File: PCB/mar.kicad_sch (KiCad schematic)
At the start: 17 parts, among them SW3 SW_DIP_x04, SW4 SW_SPDT, U18 74LS157, U19 74LS173

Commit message: Cleaned up the schematic and got started on assigning all the footprints to the symbols
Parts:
- C11: footprint (none) -> Capacitor_THT:C_Radial_D5.0mm_H5.0mm_P2.00mm
- D20, D21, D22, D23, D24, D25: footprint (none) -> LED_THT:LED_D1.8mm_W1.8mm_H2.4mm_Horizontal_O1.27mm_Z1.6mm
- R18, R19, R20, R21, R22, R23: footprint (none) -> Resistor_THT:R_Axial_DIN0207_L6.3mm_D2.5mm_P7.62mm_Horizontal
- SW3: footprint (none) -> Button_Switch_THT:SW_DIP_SPSTx04_Slide_6.7x11.72mm_W7.62mm_P2.54mm_LowProfile
- SW4: footprint (none) -> Button_Switch_SMD:SW_SPDT_CK_JS102011SAQN
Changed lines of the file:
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@@
 			)
 		)
-		(property "Footprint" ""
+		(property "Footprint" "Resistor_THT:R_Axial_DIN0207_L6.3mm_D2.5mm_P7.62mm_Horizontal"
 			(at 41.402 49.53 90)
 			(effects
@@
 			)
 		)
-		(property "Footprint" ""
+		(property "Footprint" "Resistor_THT:R_Axial_DIN0207_L6.3mm_D2.5mm_P7.62mm_Horizontal"
 			(at 23.622 49.53 90)
 			(effects
@@
 			)
 		)
-		(property "Footprint" ""
+		(property "Footprint" "Button_Switch_THT:SW_DIP_SPSTx04_Slide_6.7x11.72mm_W7.62mm_P2.54mm_LowProfile"
 			(at 66.04 86.36 0)
 			(effects
@@
 			)
 		)
-		(property "Footprint" ""
+		(property "Footprint" "Capacitor_THT:C_Radial_D5.0mm_H5.0mm_P2.00mm"
 			(at 168.6052 64.77 0)
 			(effects
@@
 			)
 		)
-		(property "Footprint" ""
+		(property "Footprint" "LED_THT:LED_D1.8mm_W1.8mm_H2.4mm_Horizontal_O1.27mm_Z1.6mm"
 			(at 43.18 39.37 0)
 			(effects
@@
 			)
 		)
-		(property "Footprint" ""
+		(property "Footprint" "Button_Switch_SMD:SW_SPDT_CK_JS102011SAQN"
 			(at 31.75 121.92 0)
 			(effects
@@
 			)
 		)
-		(property "Footprint" ""
+		(property "Footprint" "Resistor_THT:R_Axial_DIN0207_L6.3mm_D2.5mm_P7.62mm_Horizontal"
 			(at 14.732 49.53 90)
 			(effects
@@
 			)
 		)
-		(property "Footprint" ""
+		(property "Footprint" "LED_THT:LED_D1.8mm_W1.8mm_H2.4mm_Horizontal_O1.27mm_Z1.6mm"
 			(at 34.29 39.37 0)
 			(effects
@@
 			)
 		)
-		(property "Footprint" ""
+		(property "Footprint" "LED_THT:LED_D1.8mm_W1.8mm_H2.4mm_Horizontal_O1.27mm_Z1.6mm"
 			(at 25.4 39.37 0)
 			(effects
@@
 			)
 		)
-		(property "Footprint" ""
+		(property "Footprint" "LED_THT:LED_D1.8mm_W1.8mm_H2.4mm_Horizontal_O1.27mm_Z1.6mm"
 			(at 46.99 125.73 0)
 			(effects
@@
 			)
 		)
-		(property "Footprint" ""
+		(property "Footprint" "LED_THT:LED_D1.8mm_W1.8mm_H2.4mm_Horizontal_O1.27mm_Z1.6mm"
 			(at 46.99 118.11 0)
 			(effects
@@
 			)
 		)
-		(property "Footprint" ""
+		(property "Footprint" "Resistor_THT:R_Axial_DIN0207_L6.3mm_D2.5mm_P7.62mm_Horizontal"
 			(at 54.102 110.49 90)
 			(effects
@@
 			)
 		)
-		(property "Footprint" ""
+		(property "Footprint" "LED_THT:LED_D1.8mm_W1.8mm_H2.4mm_Horizontal_O1.27mm_Z1.6mm"
 			(at 16.51 39.37 0)
 			(effects
@@
 			)
 		)
-		(property "Footprint" ""
+		(property "Footprint" "Resistor_THT:R_Axial_DIN0207_L6.3mm_D2.5mm_P7.62mm_Horizontal"
 			(at 32.512 49.53 90)
 			(effects
@@
 			)
 		)
-		(property "Footprint" ""
+		(property "Footprint" "Resistor_THT:R_Axial_DIN0207_L6.3mm_D2.5mm_P7.62mm_Horizontal"
 			(at 64.262 110.49 90)
 			(effects

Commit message: added more models to work with on my pcb
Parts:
- D20, D21, D22, D23: value LED -> YELLOW; footprint LED_THT:LED_D1.8mm_W1.8mm_H2.4mm_Horizontal_O1.27mm_Z1.6mm -> LED_THT:LED_D3.0mm
- D24, D25: footprint LED_THT:LED_D1.8mm_W1.8mm_H2.4mm_Horizontal_O1.27mm_Z1.6mm -> LED_THT:LED_D3.0mm
- U18: footprint (none) -> Custom:N16
- U19: footprint (none) -> Custom:SN74LS173AN
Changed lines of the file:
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@@
 			)
 		)
-		(property "Value" "LED"
+		(property "Value" "YELLOW"
 			(at 46.99 42.2274 90)
 			(effects
@@
 			)
 		)
-		(property "Footprint" "LED_THT:LED_D1.8mm_W1.8mm_H2.4mm_Horizontal_O1.27mm_Z1.6mm"
+		(property "Footprint" "LED_THT:LED_D3.0mm"
 			(at 43.18 39.37 0)
 			(effects
@@
 			)
 		)
-		(property "Footprint" ""
+		(property "Footprint" "Custom:SN74LS173AN"
 			(at 134.62 52.07 0)
 			(effects
@@
 			)
 		)
-		(property "Footprint" ""
+		(property "Footprint" "Custom:N16"
 			(at 67.31 50.8 0)
 			(effects
@@
 			)
 		)
-		(property "Value" "LED"
+		(property "Value" "YELLOW"
 			(at 38.1 42.2274 90)
 			(effects
@@
 			)
 		)
-		(property "Footprint" "LED_THT:LED_D1.8mm_W1.8mm_H2.4mm_Horizontal_O1.27mm_Z1.6mm"
+		(property "Footprint" "LED_THT:LED_D3.0mm"
 			(at 34.29 39.37 0)
 			(effects
@@
 			)
 		)
-		(property "Value" "LED"
+		(property "Value" "YELLOW"
 			(at 29.21 42.2274 90)
 			(effects
@@
 			)
 		)
-		(property "Footprint" "LED_THT:LED_D1.8mm_W1.8mm_H2.4mm_Horizontal_O1.27mm_Z1.6mm"
+		(property "Footprint" "LED_THT:LED_D3.0mm"
 			(at 25.4 39.37 0)
 			(effects
@@
 			)
 		)
-		(property "Footprint" "LED_THT:LED_D1.8mm_W1.8mm_H2.4mm_Horizontal_O1.27mm_Z1.6mm"
+		(property "Footprint" "LED_THT:LED_D3.0mm"
 			(at 46.99 125.73 0)
 			(effects
@@
 			)
 		)
-		(property "Footprint" "LED_THT:LED_D1.8mm_W1.8mm_H2.4mm_Horizontal_O1.27mm_Z1.6mm"
+		(property "Footprint" "LED_THT:LED_D3.0mm"
 			(at 46.99 118.11 0)
 			(effects
@@
 			)
 		)
-		(property "Value" "LED"
+		(property "Value" "YELLOW"
 			(at 20.32 42.2274 90)
 			(effects
@@
 			)
 		)
-		(property "Footprint" "LED_THT:LED_D1.8mm_W1.8mm_H2.4mm_Horizontal_O1.27mm_Z1.6mm"
+		(property "Footprint" "LED_THT:LED_D3.0mm"
 			(at 16.51 39.37 0)
 			(effects

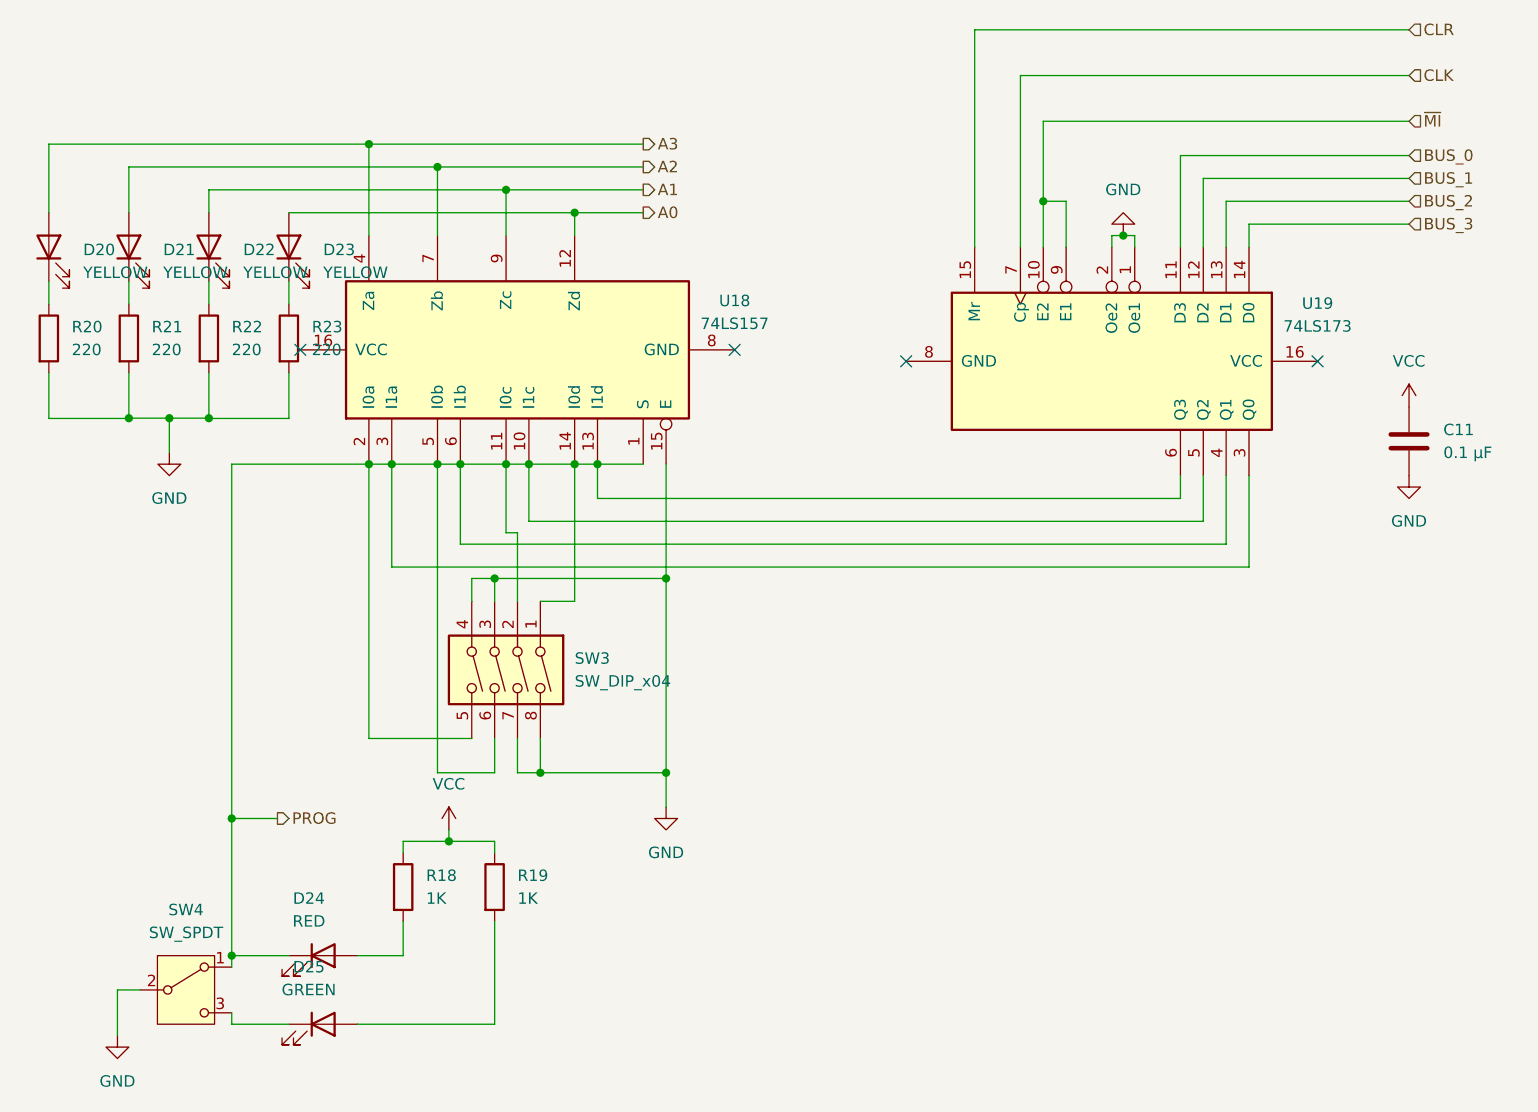
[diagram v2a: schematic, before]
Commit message: Fixed a bunch of ERC errors so know there is only one remaining.
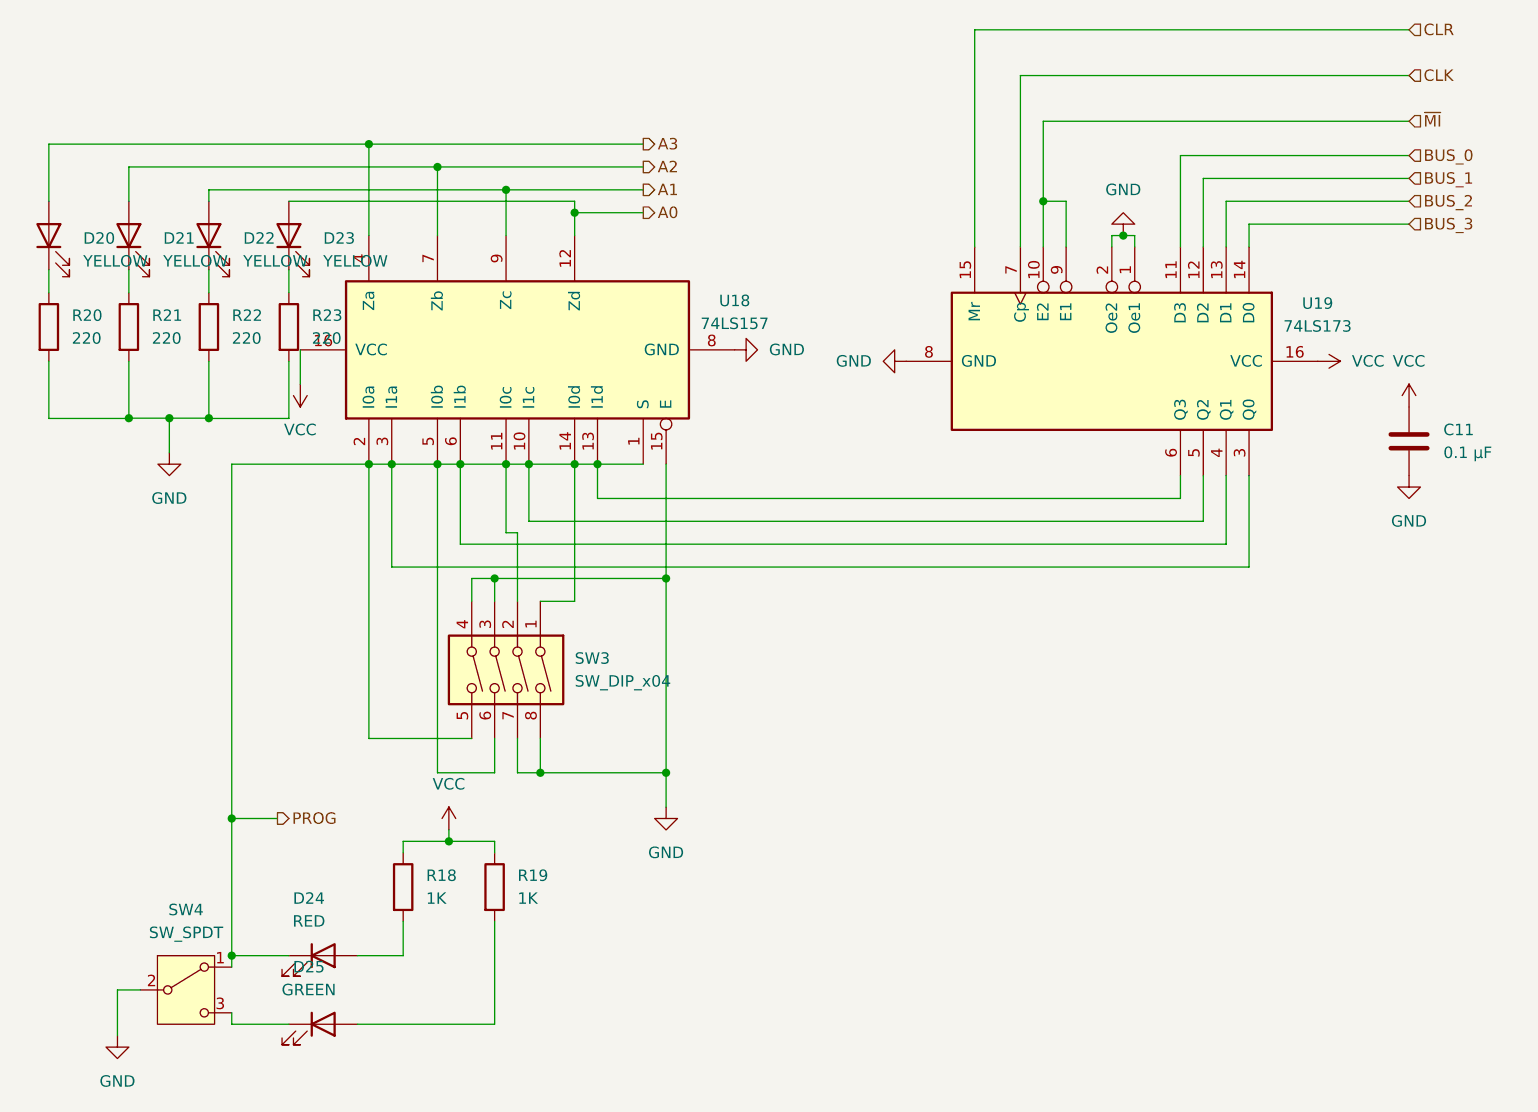
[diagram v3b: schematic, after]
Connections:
- net GND: now also U18.8 (GND), U19.8 (GND)
- net VCC: now also U18.16 (VCC), U19.16 (VCC)
- no-connect marks 4 -> 0
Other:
- moved on the sheet: D20, D21, D22, D23, R20, R21, R22, R23

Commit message: add git ignore
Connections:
- net PROG: no longer SW3.1, SW3.2, SW3.5, SW3.6, U18.10 (I1c), U18.11 (I0c), U18.13 (I1d), U18.14 (I0d), U18.2 (I0a), U18.3 (I1a), U18.5 (I0b), U18.6 (I1b), U19.3 (Q0), U19.4 (Q1), U19.5 (Q2), U19.6 (Q3)
- new net: SW3.1, U18.14 (I0d)
- new net: SW3.2, U18.11 (I0c)
- new net: SW3.5, U18.2 (I0a)
- new net: SW3.6, U18.5 (I0b)
- new net: U18.3 (I1a), U19.3 (Q0)
- new net: U18.6 (I1b), U19.4 (Q1)
- new net: U18.10 (I1c), U19.5 (Q2)
- new net: U18.13 (I1d), U19.6 (Q3)
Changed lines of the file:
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@@
-	)
-	(junction
-		(at 67.31 63.5)
-		(diameter 0)
-		(color 0 0 0 0)
 	)
 	(junction
@@
 	)
 	(junction
-		(at 54.61 63.5)
-		(diameter 0)
-		(color 0 0 0 0)
-	)
-	(junction
-		(at 69.85 63.5)
-		(diameter 0)
-		(color 0 0 0 0)
-	)
-	(junction
-		(at 74.93 63.5)
-		(diameter 0)
-		(color 0 0 0 0)
-	)
-	(junction
 		(at 71.12 97.79)
 		(diameter 0)
@@
 	)
 	(junction
-		(at 59.69 63.5)
-		(diameter 0)
-		(color 0 0 0 0)
-	)
-	(junction
 		(at 67.31 33.02)
 		(diameter 0)
@@
 	)
 	(junction
-		(at 62.23 63.5)
-		(diameter 0)
-		(color 0 0 0 0)
-	)
-	(junction
 		(at 29.899 58.3924)
 		(diameter 0)
@@
 	)
 	(junction
-		(at 52.07 63.5)
-		(diameter 0)
-		(color 0 0 0 0)
-	)
-	(junction
 		(at 66.04 76.2)
 		(diameter 0)
@@
 	)
 	(junction
-		(at 77.47 63.5)
-		(diameter 0)
-		(color 0 0 0 0)
-	)
-	(junction
 		(at 135.89 38.1)
 		(diameter 0)
@@
 	(wire
 		(pts
-			(xy 67.31 63.5) (xy 62.23 63.5)
-		)
-		(stroke
-			(width 0)
-			(type default)
-		)
-	)
-	(wire
-		(pts
 			(xy 137.16 38.1) (xy 135.89 38.1)
 		)
@@
 	(wire
 		(pts
-			(xy 36.83 63.5) (xy 36.83 102.87)
-		)
-		(stroke
-			(width 0)
-			(type default)
-		)
-	)
-	(wire
-		(pts
-			(xy 59.69 63.5) (xy 54.61 63.5)
+			(xy 82.55 66.04) (xy 36.83 66.04)
 		)
 		(stroke
@@
 	(wire
 		(pts
-			(xy 62.23 63.5) (xy 59.69 63.5)
-		)
-		(stroke
-			(width 0)
-			(type default)
-		)
-	)
-	(wire
-		(pts
 			(xy 55.88 118.11) (xy 55.88 114.3)
 		)
@@
 	(wire
 		(pts
-			(xy 69.85 63.5) (xy 67.31 63.5)
-		)
-		(stroke
-			(width 0)
-			(type default)
-		)
-	)
-	(wire
-		(pts
 			(xy 25.4 58.3924) (xy 25.4 58.42)
 		)
@@
 	(wire
 		(pts
+			(xy 82.55 63.5) (xy 82.55 66.04)
+		)
+		(stroke
+			(width 0)
+			(type default)
+		)
+	)
+	(wire
+		(pts
 			(xy 69.85 69.85) (xy 69.85 63.5)
 		)
@@
 	(wire
 		(pts
-			(xy 74.93 63.5) (xy 69.85 63.5)
-		)
-		(stroke
-			(width 0)
-			(type default)
-		)
-	)
-	(wire
-		(pts
 			(xy 127 25.4) (xy 167.64 25.4)
 		)
@@
 	(wire
 		(pts
-			(xy 77.47 63.5) (xy 74.93 63.5)
-		)
-		(stroke
-			(width 0)
-			(type default)
-		)
-	)
-	(wire
-		(pts
 			(xy 134.62 39.37) (xy 134.62 38.1)
 		)
@@
 	(wire
 		(pts
-			(xy 82.55 63.5) (xy 77.47 63.5)
-		)
-		(stroke
-			(width 0)
-			(type default)
-		)
-	)
-	(wire
-		(pts
 			(xy 68.58 93.98) (xy 68.58 97.79)
 		)
@@
 	(wire
 		(pts
-			(xy 54.61 63.5) (xy 52.07 63.5)
-		)
-		(stroke
-			(width 0)
-			(type default)
-		)
-	)
-	(wire
-		(pts
 			(xy 24.13 121.92) (xy 24.13 127)
 		)
@@
 	(wire
 		(pts
-			(xy 36.83 63.5) (xy 52.07 63.5)
-		)
-		(stroke
+			(xy 36.83 66.04) (xy 36.83 102.87)
+		)
+		(stroke

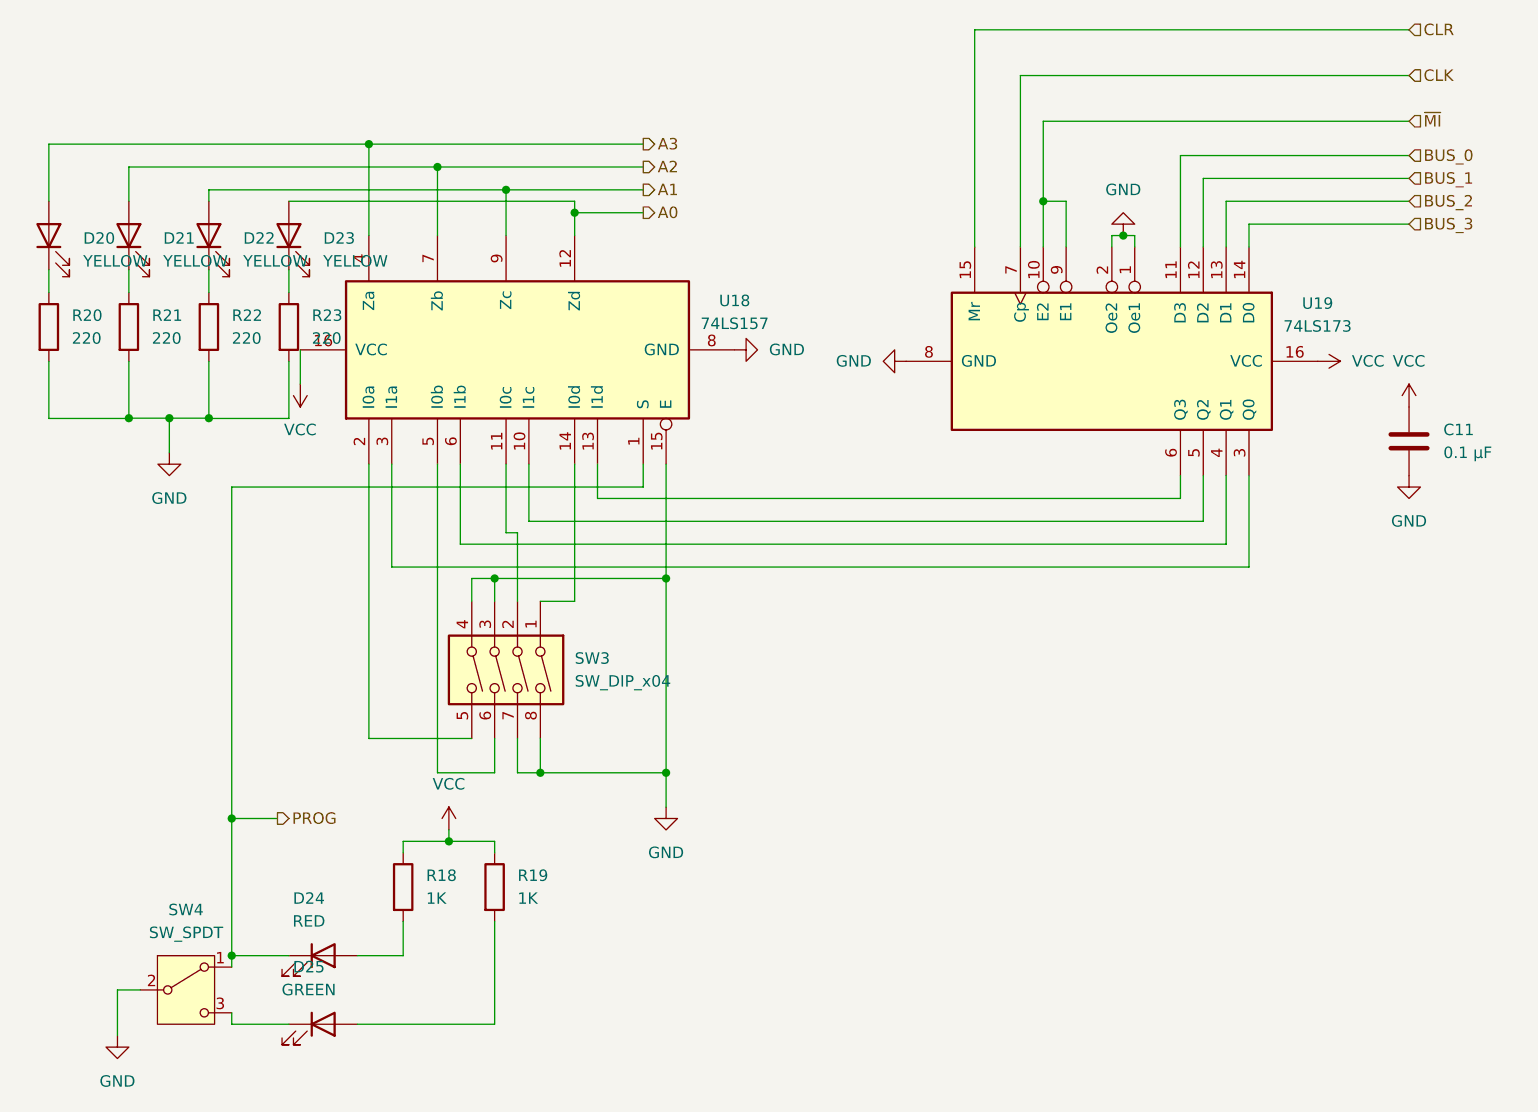
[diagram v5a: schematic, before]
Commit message: Add decupling caps and reroute pcb. Updated BOM to match new number of caps
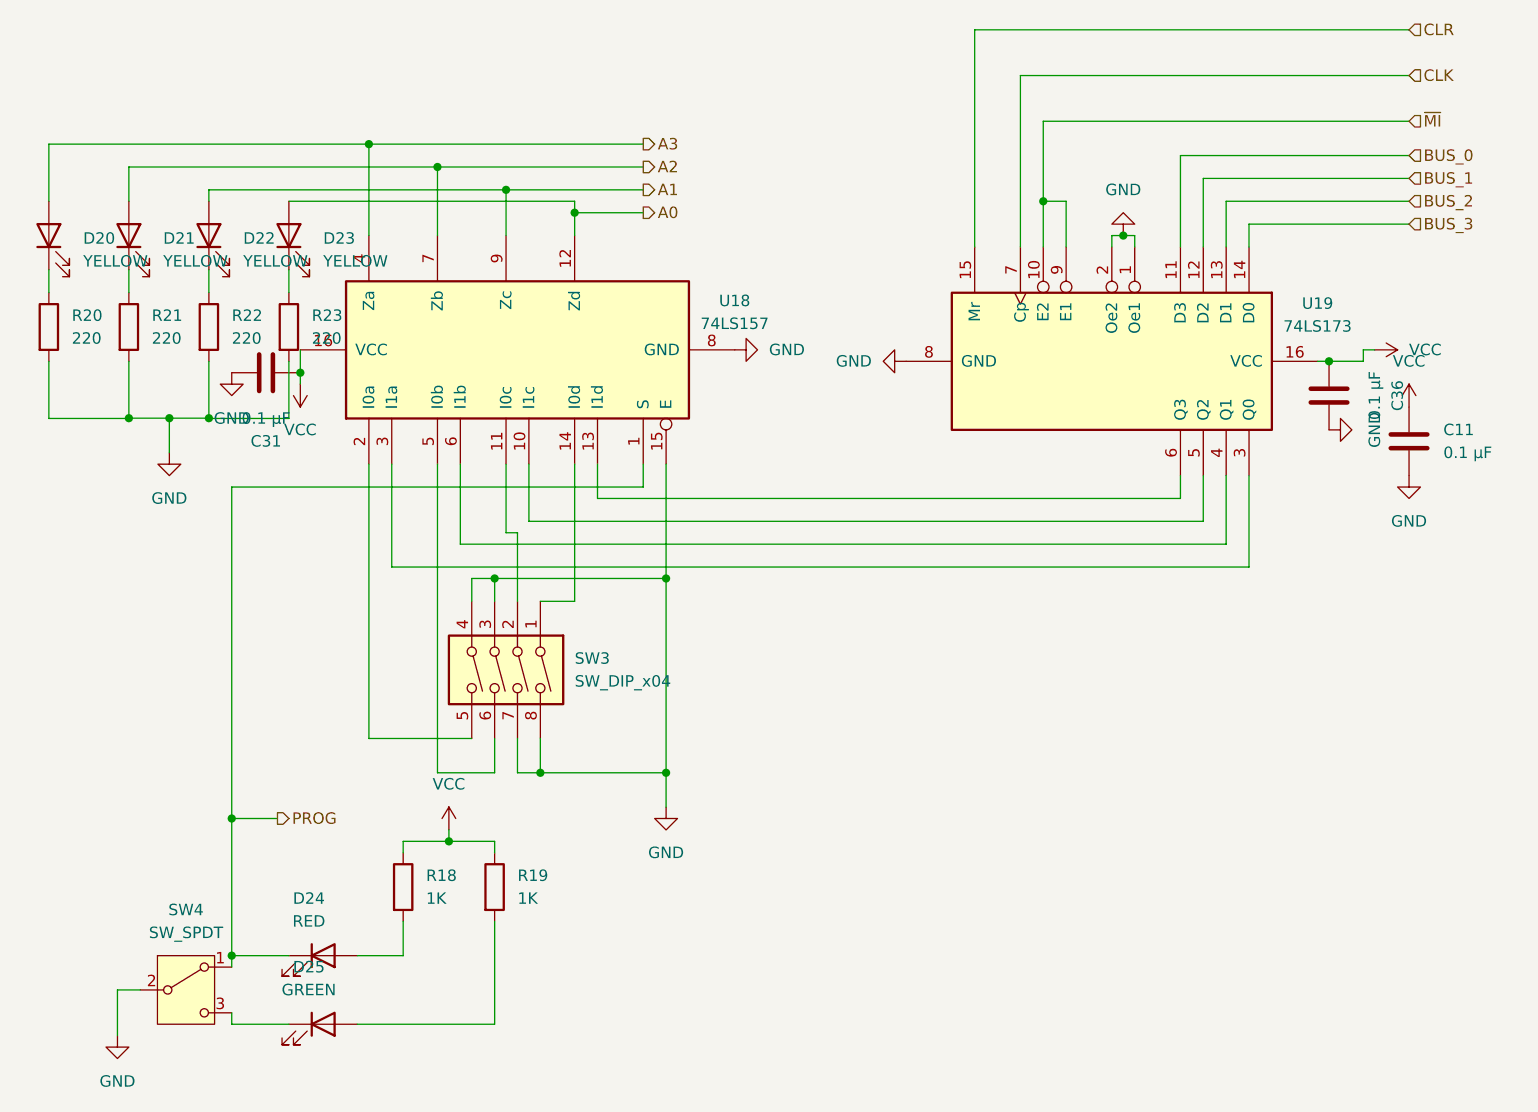
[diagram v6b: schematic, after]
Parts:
- added C31, C36: 0.1 µF, Capacitor_THT:C_Radial_D5.0mm_H5.0mm_P2.00mm, symbol Device:C
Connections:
- net GND: now also C31.2, C36.2
- net VCC: now also C31.1, C36.1
